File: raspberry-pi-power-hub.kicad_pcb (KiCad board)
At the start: 2 copper layers, 39 x 27 mm, 87 parts, among them Q1 AOD409-HXY, Q2 AOD409-HXY, Q3 NPN, SW1 TS24CA, SW2 TS24CA, SW3 TS24CA, U1 W25Q32JVSS, U3 ABM8-272-T3_C20625731, U4 RP2040, U5 AP63203WU-7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

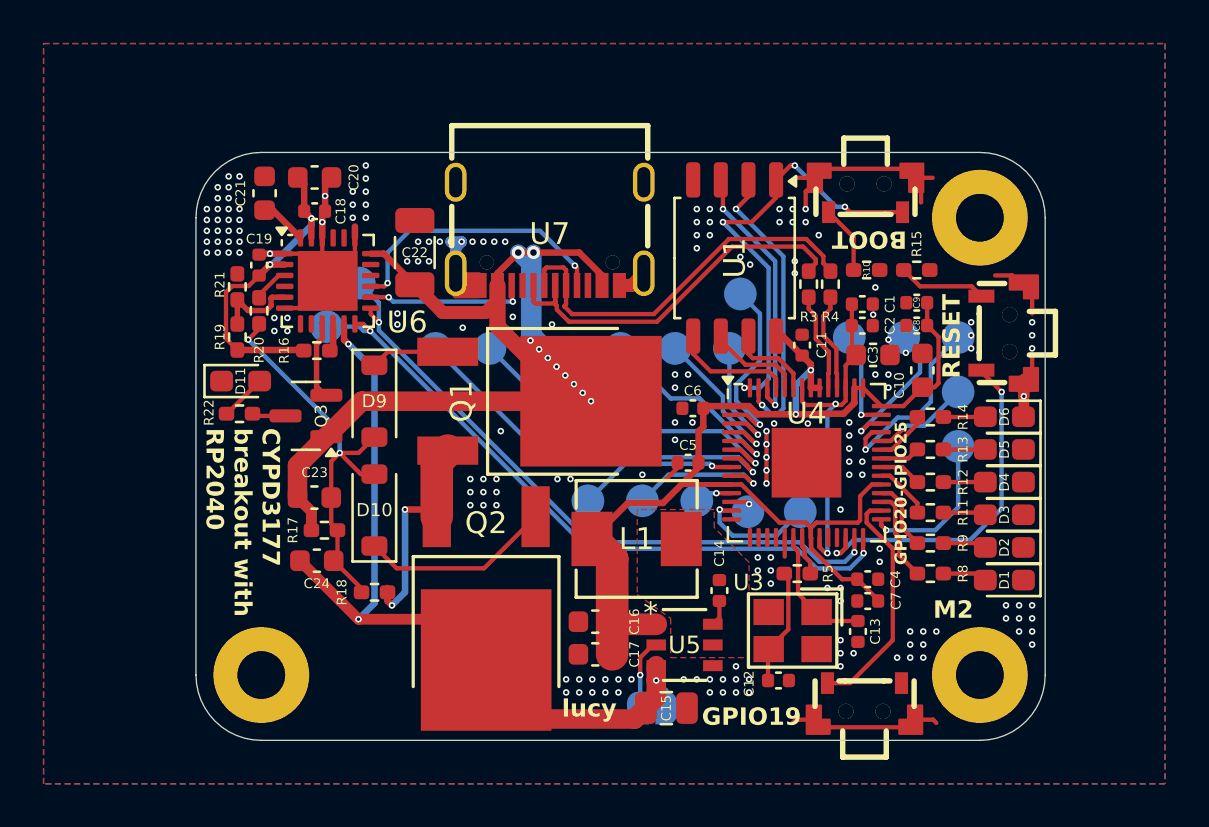
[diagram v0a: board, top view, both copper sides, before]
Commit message: fixed via size woohoo!
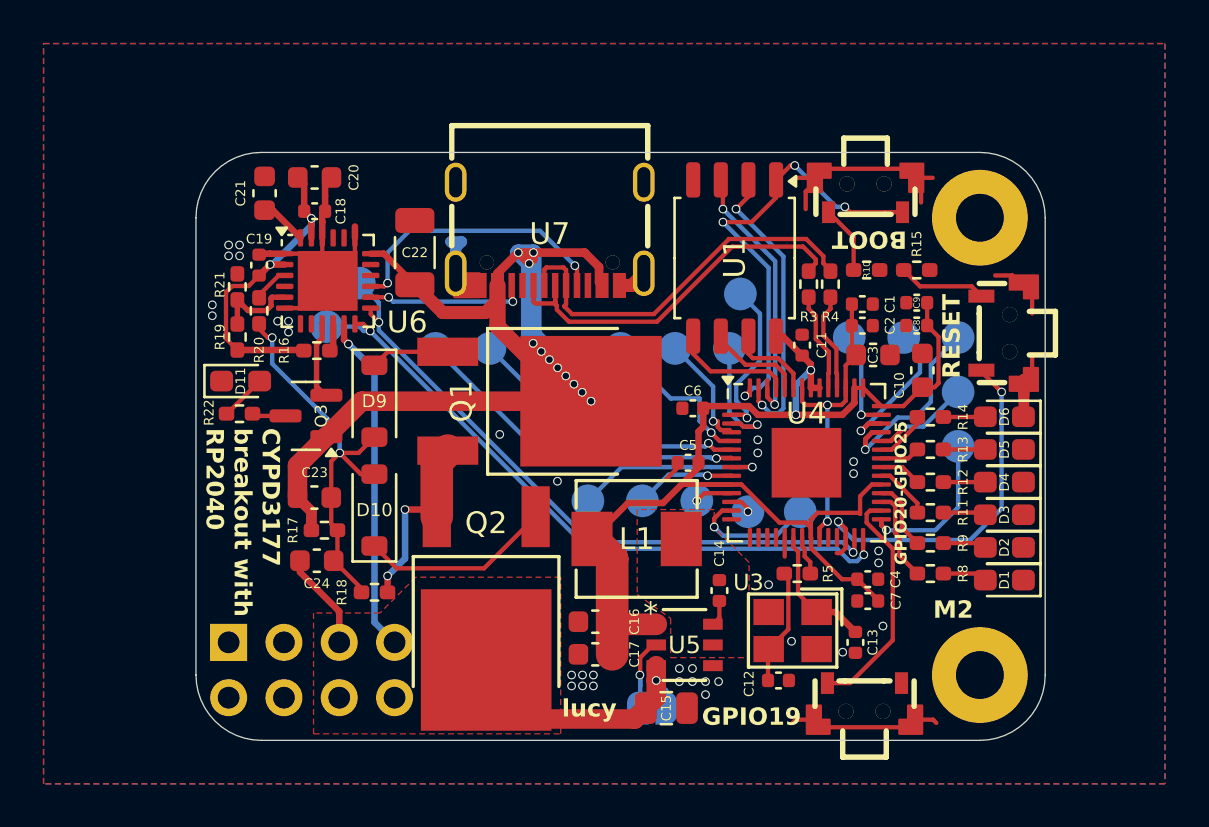
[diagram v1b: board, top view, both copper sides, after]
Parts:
- removed H4: MountingHole_Pad, MountingHole:MountingHole_2.2mm_M2_Pad
- added J1: Conn_02x04_Counter_Clockwise, Connector_PinHeader_2.54mm:PinHeader_2x04_P2.54mm_Vertical, B.Cu at (175.5, 95.5)
- moved C13 0.51 mm to (204.3, 95.5)
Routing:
- net /usb power in/USB_VBUS: track 56.5 -> 59.2 mm, vias 10 -> 11
- net GPIO4: track 15.7 -> 13.2 mm
- net GPIO5: track 18.2 -> 15.7 mm
- net GND: track 47.9 -> 45.5 mm, vias 177 -> 34
- net GPIO7: track 6.91 -> 4.62 mm
- net GPIO3: track 9.66 -> 7.47 mm
- net VBUS: track 30.7 -> 28.6 mm, vias 3 -> 2
- net GPIO2: track 7.33 -> 5.28 mm
- net GPIO6: track 7.37 -> 9.15 mm
- net /rp2040/+1.1V: track 15.4 -> 13.8 mm
- net Net-(Q1-S): track 10.4 -> 8.97 mm
- net GPIO27: track 8.74 -> 10.1 mm
- net GPIO0: track 8.76 -> 7.49 mm
- net GPIO28: track 6.80 -> 7.88 mm
- net /rp2040/RUN: track 16.1 -> 17.1 mm
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- added copper zone on F.Cu, net VBUS
